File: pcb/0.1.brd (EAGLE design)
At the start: 75 x 45 mm, 64 parts, among them Q3 BSS123, Q4 BSS123, U1 PIC18LF13K22-I/SS, U2 IR2183, U3 V_REG_317SMD, U4 INA-139, U5 INA-139, U6 INA-139, X1 TXC-7A

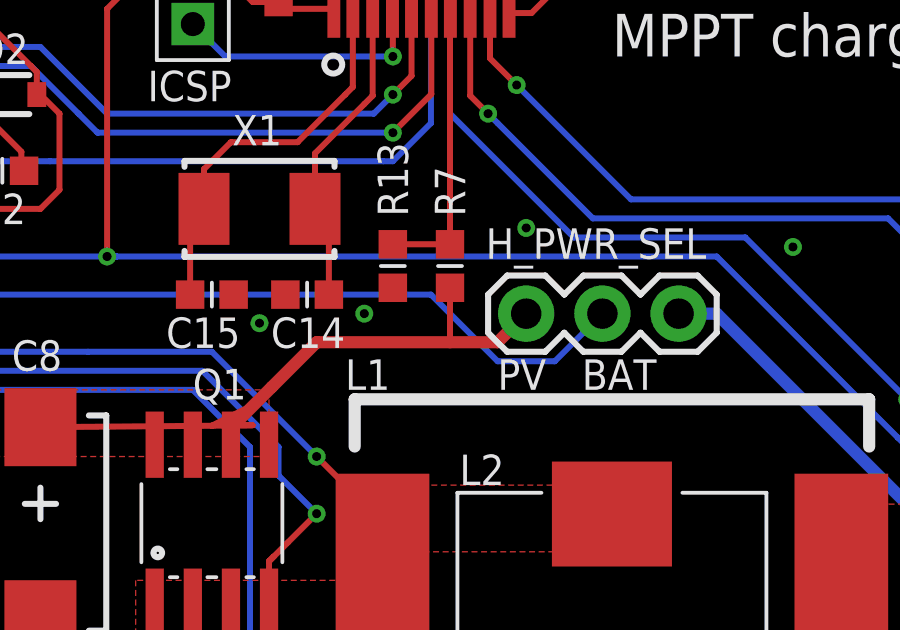
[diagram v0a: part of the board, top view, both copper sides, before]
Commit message: Removed some functions no longer used, added a few code comments, changed the file structure.
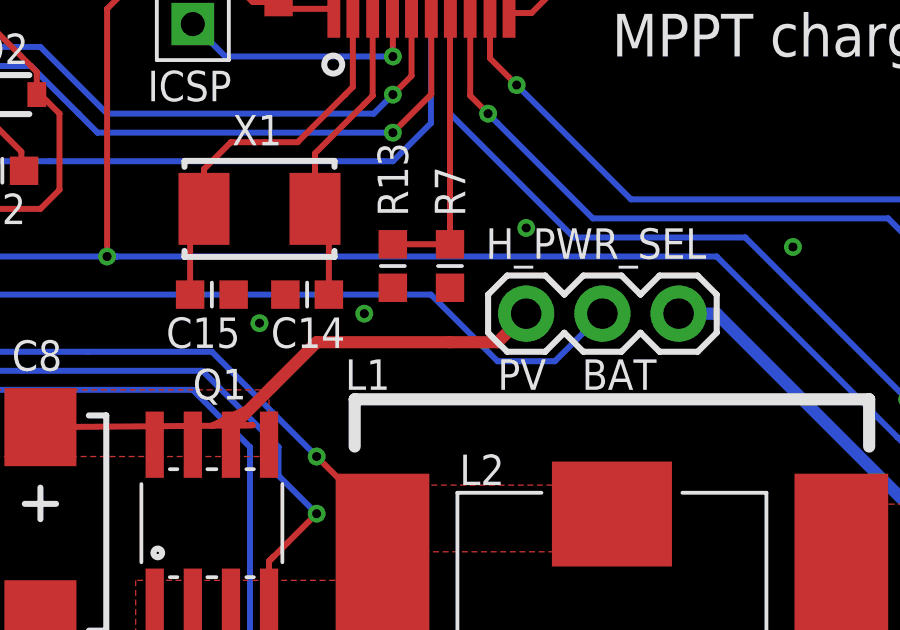
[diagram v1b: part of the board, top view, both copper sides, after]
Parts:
- C1, C6: value (none) -> 10u
- C12, C4, C7: value (none) -> 0.1u
- C13: value (none) -> 1u
- Q1, Q2: value (none) -> FDS6699
- R12, R16: value (none) -> 0
- R2: value (none) -> 220
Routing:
- net PV_IN: track 22.2 -> 20.4 mm
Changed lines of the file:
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@@
 <attribute name="VALUE" x="16.637" y="38.5445" size="0.4064" layer="27" rot="R270"/>
 </element>
-<element name="C1" library="rcl" package="C0805K" value="" x="11.1125" y="34.29" smashed="yes" rot="R270">
+<element name="C1" library="rcl" package="C0805K" value="10u" x="11.1125" y="34.29" smashed="yes" rot="R270">
 <attribute name="NAME" x="10.43" y="31.355" size="1.016" layer="25" font="vector" ratio="10"/>
 <attribute name="VALUE" x="9.2125" y="35.29" size="1.016" layer="27" rot="R270"/>
@@
 <attribute name="VALUE" x="66.167" y="17.7165" size="0.4064" layer="27" rot="R180"/>
 </element>
-<element name="C6" library="rcl" package="C0805K" value="" x="11.1125" y="38.4175" smashed="yes" rot="R90">
+<element name="C6" library="rcl" package="C0805K" value="10u" x="11.1125" y="38.4175" smashed="yes" rot="R90">
 <attribute name="NAME" x="10.43" y="40.5625" size="1.016" layer="25" font="vector" ratio="10"/>
 <attribute name="VALUE" x="13.0125" y="37.4175" size="1.016" layer="27" rot="R90"/>
@@
 <attribute name="NAME" x="13.335" y="30.7975" size="1.016" layer="25" font="vector" ratio="10"/>
 </element>
-<element name="R12" library="01-eos-components" package="0603" value="" x="13.0175" y="24.13" smashed="yes" rot="R90">
+<element name="R12" library="01-eos-components" package="0603" value="0" x="13.0175" y="24.13" smashed="yes" rot="R90">
 <attribute name="NAME" x="15.113" y="22.9235" size="1.016" layer="25" font="vector" ratio="10" rot="R90"/>
 <attribute name="VALUE" x="14.1605" y="23.114" size="0.4064" layer="27" font="vector" rot="R90"/>
 </element>
-<element name="R16" library="01-eos-components" package="0603" value="" x="11.1125" y="24.13" smashed="yes" rot="R90">
+<element name="R16" library="01-eos-components" package="0603" value="0" x="11.1125" y="24.13" smashed="yes" rot="R90">
 <attribute name="NAME" x="10.033" y="22.9235" size="1.016" layer="25" font="vector" ratio="10" rot="R90"/>
 <attribute name="VALUE" x="12.2555" y="23.114" size="0.4064" layer="27" font="vector" rot="R90"/>
@@
 <attribute name="VALUE" x="69.85" y="6.985" size="0.4064" layer="27" rot="R90"/>
 </element>
-<element name="C4" library="01-eos-components" package="0603" value="" x="4.1275" y="18.7325" smashed="yes">
+<element name="C4" library="01-eos-components" package="0603" value="0.1u" x="4.1275" y="18.7325" smashed="yes">
 <attribute name="NAME" x="2.6035" y="19.4945" size="1.016" layer="25" font="vector" ratio="10"/>
 <attribute name="VALUE" x="3.1115" y="17.5895" size="0.4064" layer="27" font="vector"/>
 </element>
-<element name="C7" library="01-eos-components" package="0603" value="" x="53.975" y="20.6375" smashed="yes" rot="R270">
+<element name="C7" library="01-eos-components" package="0603" value="0.1u" x="53.975" y="20.6375" smashed="yes" rot="R270">
 <attribute name="NAME" x="53.4035" y="22.352" size="1.016" layer="25" font="vector" ratio="10"/>
 <attribute name="VALUE" x="52.832" y="21.6535" size="0.4064" layer="27" font="vector" rot="R270"/>
 </element>
-<element name="C12" library="01-eos-components" package="0603" value="" x="60.96" y="22.5425" smashed="yes" rot="R270">
+<element name="C12" library="01-eos-components" package="0603" value="0.1u" x="60.96" y="22.5425" smashed="yes" rot="R270">
 <attribute name="NAME" x="62.2935" y="22.6695" size="1.016" layer="25" font="vector" ratio="10"/>
 <attribute name="VALUE" x="59.817" y="23.5585" size="0.4064" layer="27" font="vector" rot="R270"/>
@@
 <attribute name="VALUE" x="8.5725" y="26.035" size="1.016" layer="27" font="vector" ratio="10" rot="R90"/>
 </element>
-<element name="R2" library="01-eos-components" package="0603" value="" x="26.035" y="43.18" smashed="yes" rot="R180">
+<element name="R2" library="01-eos-components" package="0603" value="220" x="26.035" y="43.18" smashed="yes" rot="R180">
 <attribute name="NAME" x="27.686" y="42.672" size="1.016" layer="25" font="vector" ratio="10"/>
 <attribute name="VALUE" x="27.051" y="44.323" size="0.4064" layer="27" font="vector" rot="R180"/>
@@
 <element name="U$3" library="01-eos-components" package="CORNER_SCREW" value="CORNER_SCREW" x="75" y="45" smashed="yes" rot="R180"/>
 <element name="U$4" library="01-eos-components" package="CORNER_SCREW" value="CORNER_SCREW" x="0" y="45" smashed="yes" rot="R270"/>
-<element name="Q1" library="01-eos-components" package="SO08" value="" x="26.67" y="15.875" smashed="yes">
+<element name="Q1" library="01-eos-components" package="SO08" value="FDS6699" x="26.67" y="15.875" smashed="yes">
 <attribute name="VALUE" x="24.13" y="10.16" size="1.016" layer="27" font="vector" ratio="10"/>
 <attribute name="NAME" x="26.035" y="20.0025" size="1.016" layer="25" font="vector" ratio="10"/>
 </element>
-<element name="Q2" library="01-eos-components" package="SO08" value="" x="26.67" y="6.985" smashed="yes">
+<element name="Q2" library="01-eos-components" package="SO08" value="FDS6699" x="26.67" y="6.985" smashed="yes">
 <attribute name="VALUE" x="24.13" y="1.27" size="1.016" layer="27" font="vector" ratio="10"/>
 <attribute name="NAME" x="26.035" y="1.27" size="1.016" layer="25" font="vector" ratio="10"/>
@@
 <attribute name="VALUE" x="63.373" y="11.4935" size="0.4064" layer="27"/>
 </element>
-<element name="C13" library="01-eos-components" package="0603" value="" x="28.8925" y="33.9725" smashed="yes" rot="R270">
+<element name="C13" library="01-eos-components" package="0603" value="1u" x="28.8925" y="33.9725" smashed="yes" rot="R270">
 <attribute name="NAME" x="29.4005" y="35.6235" size="1.016" layer="25" font="vector" ratio="10" rot="R90"/>
 <attribute name="VALUE" x="27.7495" y="34.9885" size="0.4064" layer="27" font="vector" rot="R270"/>
@@
 <signal name="PV_IN">
 <contactref element="H_PWR_SEL" pad="3"/>
-<contactref element="RS1" pad="1"/>
-<contactref element="U4" pad="4"/>
-<contactref element="R7" pad="2"/>
 <contactref element="C8" pad="+"/>
 <contactref element="C9" pad="+"/>
@@
 <wire x1="36.195" y1="21.9075" x2="37.1475" y2="22.86" width="0.4064" layer="1"/>
 <wire x1="27.94" y1="19.7626" x2="26.6650375" y2="19.1226375" width="0.2" layer="1"/>
-<wire x1="34.6075" y1="23.7225" x2="34.6075" y2="21.9075" width="0.2" layer="1"/>
 <contactref element="Q1" pad="5"/>
 <contactref element="Q1" pad="6"/>
 <contactref element="Q1" pad="7"/>
 <contactref element="Q1" pad="8"/>
+<contactref element="RS1" pad="1"/>
+<contactref element="U4" pad="4"/>
+<contactref element="R7" pad="2"/>
+<wire x1="34.6075" y1="21.9075" x2="34.6075" y2="23.7225" width="0" layer="19" extent="1-1"/>
+<wire x1="27.305" y1="18.4912" x2="27.395" y2="19.14" width="0" layer="19" extent="1-1"/>
+<wire x1="28.575" y1="18.4912" x2="28.03" y2="19.14" width="0" layer="19" extent="1-1"/>
+<wire x1="26.035" y1="18.4912" x2="26.6650375" y2="19.1226375" width="0" layer="19" extent="1-1"/>
+<wire x1="24.765" y1="18.4912" x2="26.035" y2="18.4912" width="0" layer="19" extent="1-1"/>
+<wire x1="15.24" y1="19.075" x2="20.955" y2="19.075" width="0" layer="19" extent="1-1"/>
+<wire x1="10.795" y1="18.52" x2="15.24" y2="19.075" width="0" layer="19" extent="1-1"/>
+<wire x1="8.57" y1="18.4451" x2="10.795" y2="18.52" width="0" layer="19" extent="1-1"/>
 </signal>
 <signal name="BAT">
